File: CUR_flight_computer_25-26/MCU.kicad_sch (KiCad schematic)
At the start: 28 parts, among them SW1 GSPTS0018, SW2 GSPTS0018, U1 STM32H523VETx, Y1 16M18PX/XT324-10/10

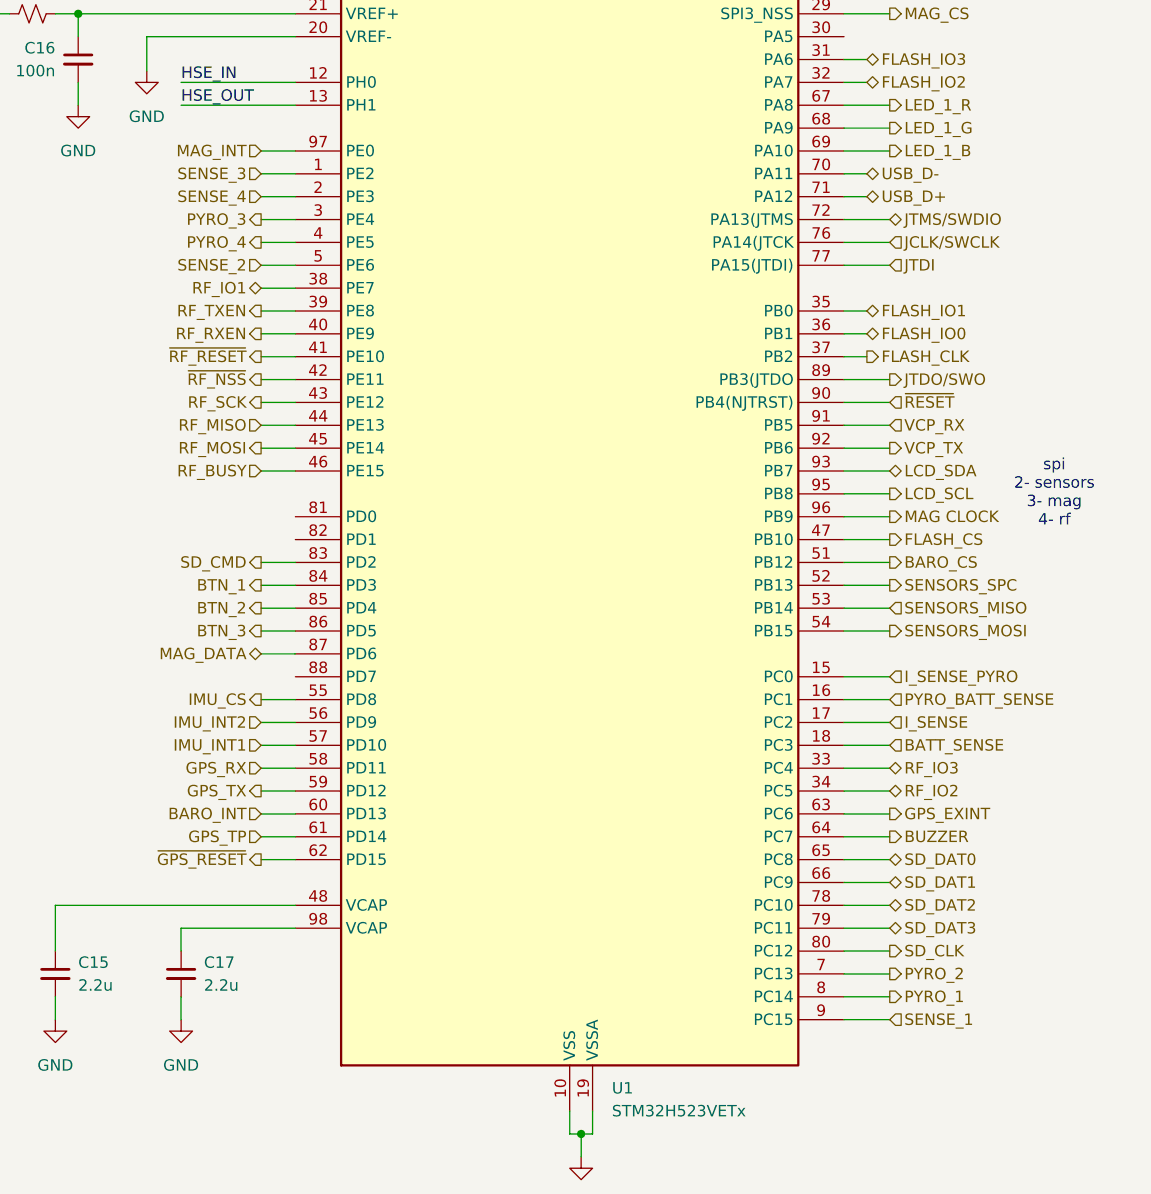
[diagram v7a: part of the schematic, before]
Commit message: RF and Pyros routed
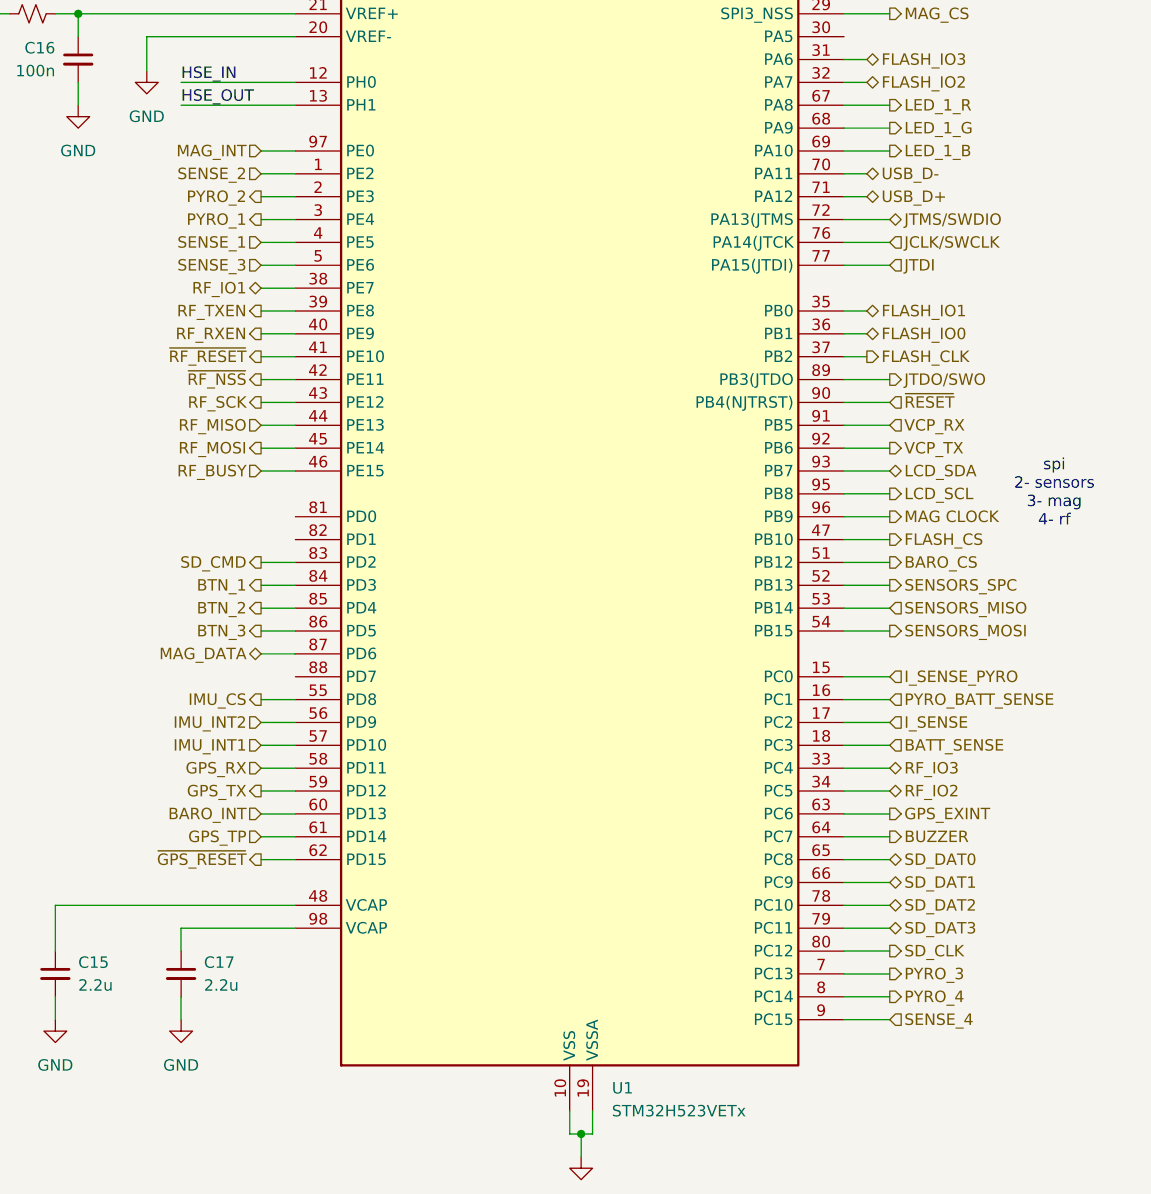
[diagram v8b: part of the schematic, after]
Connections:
- net PYRO_1: now also U1.3 (PE4); no longer U1.8 (PC14)
- net PYRO_2: now also U1.2 (PE3); no longer U1.7 (PC13)
- net PYRO_3: now also U1.7 (PC13); no longer U1.3 (PE4)
- net PYRO_4: now also U1.8 (PC14); no longer U1.4 (PE5)
- net SENSE_1: now also U1.4 (PE5); no longer U1.9 (PC15)
- net SENSE_2: now also U1.1 (PE2); no longer U1.5 (PE6)
- net SENSE_3: now also U1.5 (PE6); no longer U1.1 (PE2)
- net SENSE_4: now also U1.9 (PC15); no longer U1.2 (PE3)
